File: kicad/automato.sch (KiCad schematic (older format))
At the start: 73 parts, among them J1 USB_C_Receptacle, J10 QWIIC 0, J11 UART2, J12 STEMMA 0, J2 LiPo, J3 Conn_01x07_Male, J4 Screw_Terminal_01x14, J5 USB_C_Receptacle, J6 Conn_Coaxial, J7 1-WIRE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

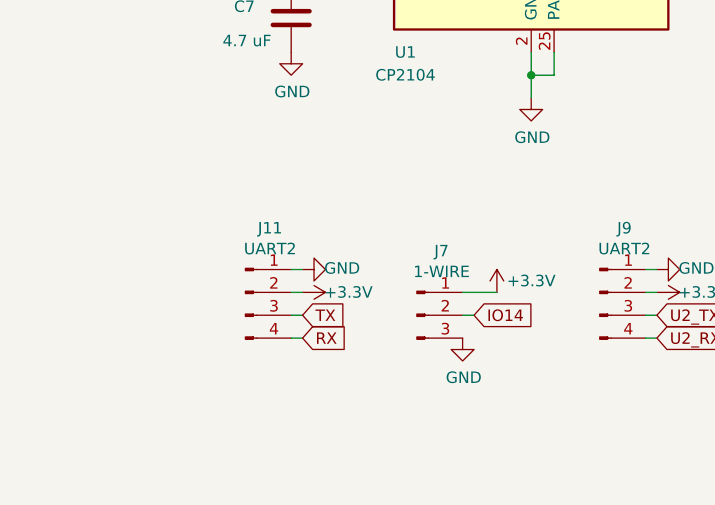
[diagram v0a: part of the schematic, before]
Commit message: remove usb-c uart JST
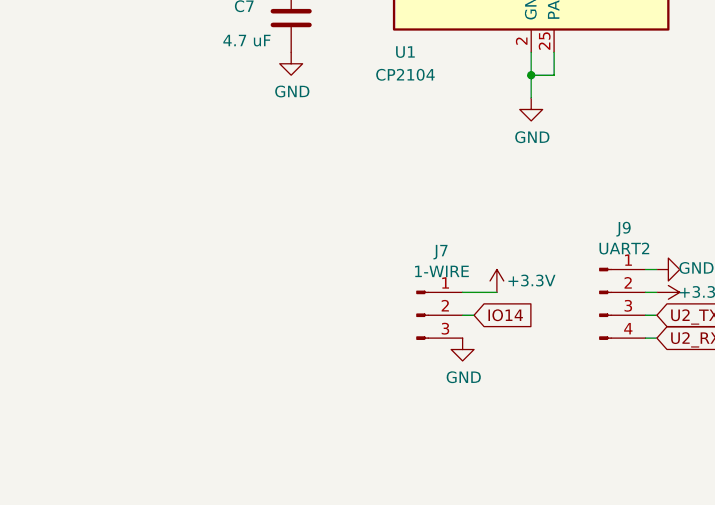
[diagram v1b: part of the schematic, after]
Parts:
- removed J11: UART2, Connector_JST:JST_PH_S4B-PH-SM4-TB_1x04-1MP_P2.00mm_Horizontal, symbol Connector:Conn_01x04_Male
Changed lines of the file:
@@
 	3500 9650 3450 9650
-$Comp
-L power:GND #PWR0114
-U 1 1 63277429
-P 1950 9350
-F 0 "#PWR0114" H 1950 9100 50  0001 C CNN
-F 1 "GND" V 1955 9177 50  0000 C CNN
-F 2 "" H 1950 9350 50  0001 C CNN
-F 3 "" H 1950 9350 50  0001 C CNN
-	1    1950 9350
-	0    -1   -1   0
-$EndComp
-Text GLabel 1950 9650 2    50   Input ~ 0
-RX
-Text GLabel 1950 9550 2    50   Input ~ 0
-TX
-Wire Wire Line
-	1950 9550 1900 9550
-Wire Wire Line
-	1950 9450 1900 9450
-$Comp
-L Connector:Conn_01x04_Male J11
-U 1 1 63277433
-P 1700 9450
-F 0 "J11" H 1808 9731 50  0000 C CNN
-F 1 "UART2" H 1808 9640 50  0000 C CNN
-F 2 "Connector_JST:JST_PH_S4B-PH-SM4-TB_1x04-1MP_P2.00mm_Horizontal" H 1700 9450 50  0001 C CNN
-F 3 "~" H 1700 9450 50  0001 C CNN
-	1    1700 9450
-	1    0    0    -1
-$EndComp
-$Comp
-L power:+3.3V #PWR0115
-U 1 1 63277439
-P 1950 9450
-F 0 "#PWR0115" H 1950 9300 50  0001 C CNN
-F 1 "+3.3V" V 1950 9650 50  0000 C CNN
-F 2 "" H 1950 9450 50  0001 C CNN
-F 3 "" H 1950 9450 50  0001 C CNN
-	1    1950 9450
-	0    1    1    0
-$EndComp
-Wire Wire Line
-	1900 9350 1950 9350
-Wire Wire Line
-	1950 9650 1900 9650
 $Comp
 L power:+3.3V #PWR0116

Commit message: add i2c and uart level shifting
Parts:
- added JP? (x3): SolderJumper_3_Bridged12, Jumper:SolderJumper-3_P1.3mm_Bridged12_RoundedPad1.0x1.5mm, symbol Jumper:SolderJumper_3_Bridged12
- added Q4, Q? (x4): Q_DUAL_NMOS_S1G1D2S2G2D1, Package_TO_SOT_SMD:SOT-23-6, symbol Device:Q_DUAL_NMOS_S1G1D2S2G2D1
- added Q?: Q_NMOS_GDS, symbol Device:Q_NMOS_GDS
- added RN1, RN? (x2): R_Pack02, Resistor_SMD:R_Array_Concave_2x0603, symbol Device:R_Pack02
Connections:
- wire segments 265 -> 304
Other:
- moved on the sheet: J10, J12, J4, J7, J9

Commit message: spaced out power supplies
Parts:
- gave numbers to parts that had none: 8
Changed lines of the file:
@@
 I2C_SCL
 $Comp
-L Jumper:SolderJumper_3_Bridged12 JP?
+L Jumper:SolderJumper_3_Bridged12 JP5
 U 1 1 6348EF51
 P 7450 9450
-F 0 "JP?" V 7404 9518 50  0000 L CNN
+F 0 "JP5" V 7404 9518 50  0000 L CNN
 F 1 "SolderJumper_3_Bridged12" V 7495 9518 50  0000 L CNN
 F 2 "Jumper:SolderJumper-3_P1.3mm_Bridged12_RoundedPad1.0x1.5mm" H 7450 9450 50  0001 C CNN
@@
 Connection ~ 7450 9600
 $Comp
-L power:+3.3V #PWR?
+L power:+3.3V #PWR0106
 U 1 1 634E420B
 P 7250 9250
-F 0 "#PWR?" H 7250 9100 50  0001 C CNN
+F 0 "#PWR0106" H 7250 9100 50  0001 C CNN
 F 1 "+3.3V" H 7400 9300 50  0000 C CNN
 F 2 "" H 7250 9250 50  0001 C CNN
@@
 	7100 10150 7700 10150
 $Comp
-L power:GND #PWR?
+L power:GND #PWR0107
 U 1 1 63571987
 P 4900 9850
-F 0 "#PWR?" H 4900 9600 50  0001 C CNN
+F 0 "#PWR0107" H 4900 9600 50  0001 C CNN
 F 1 "GND" V 4850 9850 50  0000 C CNN
 F 2 "" H 4900 9850 50  0001 C CNN
@@
 $EndComp
 $Comp
-L Device:Q_DUAL_NMOS_S1G1D2S2G2D1 Q?
+L Device:Q_DUAL_NMOS_S1G1D2S2G2D1 Q7
 U 1 1 6357198D
 P 5650 10050
-F 0 "Q?" V 5899 10050 50  0000 C CNN
+F 0 "Q7" V 5899 10050 50  0000 C CNN
 F 1 "Q_DUAL_NMOS_S1G1D2S2G2D1" V 5990 10050 50  0000 C CNN
 F 2 "Package_TO_SOT_SMD:SOT-23-6" H 5850 10050 50  0001 C CNN
@@
 	6200 10050 6250 10050
 $Comp
-L power:+3.3V #PWR?
+L power:+3.3V #PWR0108
 U 1 1 63571997
 P 5650 9600
-F 0 "#PWR?" H 5650 9450 50  0001 C CNN
+F 0 "#PWR0108" H 5650 9450 50  0001 C CNN
 F 1 "+3.3V" H 5800 9650 50  0000 C CNN
 F 2 "" H 5650 9600 50  0001 C CNN
@@
 	5650 9600 5650 9850
 $Comp
-L power:+3.3V #PWR?
+L power:+3.3V #PWR0110
 U 1 1 6357199E
 P 6000 9600
-F 0 "#PWR?" H 6000 9450 50  0001 C CNN
+F 0 "#PWR0110" H 6000 9450 50  0001 C CNN
 F 1 "+3.3V" H 6150 9650 50  0000 C CNN
 F 2 "" H 6000 9600 50  0001 C CNN
@@
 	5850 10150 6250 10150
 $Comp
-L Device:Q_DUAL_NMOS_S1G1D2S2G2D1 Q?
+L Device:Q_DUAL_NMOS_S1G1D2S2G2D1 Q7
 U 2 1 635719A9
 P 6000 9950
-F 0 "Q?" V 6249 9950 50  0000 C CNN
+F 0 "Q7" V 6249 9950 50  0000 C CNN
 F 1 "Q_DUAL_NMOS_S1G1D2S2G2D1" V 6340 9950 50  0000 C CNN
 F 2 "Package_TO_SOT_SMD:SOT-23-6" H 6200 9950 50  0001 C CNN
@@
 $EndComp
 $Comp
-L Device:R_Pack02 RN?
+L Device:R_Pack02 RN3
 U 1 1 635719AF
 P 5400 9800
-F 0 "RN?" H 5488 9846 50  0000 L CNN
+F 0 "RN3" H 5488 9846 50  0000 L CNN
 F 1 "R_Pack02" H 5488 9755 50  0000 L CNN
 F 2 "Resistor_SMD:R_Array_Concave_2x0603" V 5575 9800 50  0001 C CNN
@@
 I2C_SCL
 $Comp
-L Jumper:SolderJumper_3_Bridged12 JP?
+L Jumper:SolderJumper_3_Bridged12 JP4
 U 1 1 635719B7
 P 5050 9450
-F 0 "JP?" V 5004 9518 50  0000 L CNN
+F 0 "JP4" V 5004 9518 50  0000 L CNN
 F 1 "SolderJumper_3_Bridged12" V 5095 9518 50  0000 L CNN
 F 2 "Jumper:SolderJumper-3_P1.3mm_Bridged12_RoundedPad1.0x1.5mm" H 5050 9450 50  0001 C CNN
@@
 Connection ~ 5050 9600
 $Comp
-L power:+3.3V #PWR?
+L power:+3.3V #PWR0113
 U 1 1 635719C3
 P 4850 9250
-F 0 "#PWR?" H 4850 9100 50  0001 C CNN
+F 0 "#PWR0113" H 4850 9100 50  0001 C CNN
 F 1 "+3.3V" H 5000 9300 50  0000 C CNN
 F 2 "" H 4850 9250 50  0001 C CNN
@@
 	2400 9850 2600 9850
 $Comp
-L power:GND #PWR?
+L power:GND #PWR0118
 U 1 1 63640A07
 P 2600 9850
-F 0 "#PWR?" H 2600 9600 50  0001 C CNN
+F 0 "#PWR0118" H 2600 9600 50  0001 C CNN
 F 1 "GND" V 2550 9850 50  0000 C CNN
 F 2 "" H 2600 9850 50  0001 C CNN
@@
 $EndComp
 $Comp
-L Device:Q_DUAL_NMOS_S1G1D2S2G2D1 Q?
+L Device:Q_DUAL_NMOS_S1G1D2S2G2D1 Q6
 U 1 1 63640A0D
 P 3350 10050
-F 0 "Q?" V 3599 10050 50  0000 C CNN
+F 0 "Q6" V 3599 10050 50  0000 C CNN
 F 1 "Q_DUAL_NMOS_S1G1D2S2G2D1" V 3690 10050 50  0000 C CNN
 F 2 "Package_TO_SOT_SMD:SOT-23-6" H 3550 10050 50  0001 C CNN
@@
 	3900 10050 3950 10050
 $Comp
-L power:+3.3V #PWR?
+L power:+3.3V #PWR0119
 U 1 1 63640A17
 P 3350 9600
-F 0 "#PWR?" H 3350 9450 50  0001 C CNN
+F 0 "#PWR0119" H 3350 9450 50  0001 C CNN
 F 1 "+3.3V" H 3500 9650 50  0000 C CNN
 F 2 "" H 3350 9600 50  0001 C CNN
@@
 	3350 9600 3350 9850
 $Comp
-L power:+3.3V #PWR?
+L power:+3.3V #PWR0120
 U 1 1 63640A1E
 P 3700 9600
-F 0 "#PWR?" H 3700 9450 50  0001 C CNN
+F 0 "#PWR0120" H 3700 9450 50  0001 C CNN
 F 1 "+3.3V" H 3850 9650 50  0000 C CNN
 F 2 "" H 3700 9600 50  0001 C CNN
@@
 	3550 10150 3950 10150
 $Comp
-L Device:Q_DUAL_NMOS_S1G1D2S2G2D1 Q?
+L Device:Q_DUAL_NMOS_S1G1D2S2G2D1 Q6
 U 2 1 63640A29
 P 3700 9950
-F 0 "Q?" V 3949 9950 50  0000 C CNN
+F 0 "Q6" V 3949 9950 50  0000 C CNN
 F 1 "Q_DUAL_NMOS_S1G1D2S2G2D1" V 4040 9950 50  0000 C CNN
 F 2 "Package_TO_SOT_SMD:SOT-23-6" H 3900 9950 50  0001 C CNN
@@
 $EndComp
 $Comp
-L Device:R_Pack02 RN?
+L Device:R_Pack02 RN2
 U 1 1 63640A2F
 P 3100 9800
-F 0 "RN?" H 3188 9846 50  0000 L CNN
+F 0 "RN2" H 3188 9846 50  0000 L CNN
 F 1 "R_Pack02" H 3188 9755 50  0000 L CNN
 F 2 "Resistor_SMD:R_Array_Concave_2x0603" V 3275 9800 50  0001 C CNN
@@
 $EndComp
 $Comp
-L Jumper:SolderJumper_3_Bridged12 JP?
+L Jumper:SolderJumper_3_Bridged12 JP3
 U 1 1 63640A37
 P 2750 9450
-F 0 "JP?" V 2704 9518 50  0000 L CNN
+F 0 "JP3" V 2704 9518 50  0000 L CNN
 F 1 "SolderJumper_3_Bridged12" V 2795 9518 50  0000 L CNN
 F 2 "Jumper:SolderJumper-3_P1.3mm_Bridged12_RoundedPad1.0x1.5mm" H 2750 9450 50  0001 C CNN
@@
 Connection ~ 2750 9600
 $Comp
-L power:+3.3V #PWR?
+L power:+3.3V #PWR0121
 U 1 1 63640A43
 P 2550 9250
-F 0 "#PWR?" H 2550 9100 50  0001 C CNN
+F 0 "#PWR0121" H 2550 9100 50  0001 C CNN
 F 1 "+3.3V" H 2700 9300 50  0000 C CNN
 F 2 "" H 2550 9250 50  0001 C CNN
@@
 U2_RXD
 $Comp
-L Device:Q_NMOS_GDS Q?
+L Device:Q_NMOS_GDS Q5
 U 1 1 637094B9
 P 1400 9400
-F 0 "Q?" V 1649 9400 50  0000 C CNN
+F 0 "Q5" V 1649 9400 50  0000 C CNN
 F 1 "Q_NMOS_GDS" V 1740 9400 50  0000 C CNN
 F 2 "" H 1600 9500 50  0001 C CNN

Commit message: writing in wroom-da
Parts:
- removed Q5: Q_NMOS_GDS, symbol Device:Q_NMOS_GDS
- added U8: ESP32-WROOM-DA, automato-sensor:ESP32-WROOM-DA, symbol automato-sensor:ESP32-WROOM-DA
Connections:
- wire segments 304 -> 341

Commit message: playing with pins
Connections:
- net CS_RELAY: now also U8.17 (IO13); no longer U8.14 (IO12)
- net CS_SD: now also U8.14 (IO12); no longer U8.31 (IO5)
- net I2C_SCL: now also U8.38 (IO22); no longer U8.35 (IO21)
- net I2C_SDA: now also U8.35 (IO21); no longer U8.33 (IO19)
- net IO13: no longer U4.13 (IO14), U8.17 (IO13)
- net IO14: now also U4.13 (IO14); no longer U4.23 (IO15)
- net IO15: now also U4.23 (IO15); no longer JP1.3 (B), Q6.1 (S), U4.27 (IO16)
- net IO16: now also JP1.3 (B), Q6.1 (S), U4.27 (IO16); no longer JP2.3 (B), Q6.4 (S), U4.28 (IO17)
- net IRQ_LORA: now also U8.31 (IO5); no longer U8.9 (IO33)
- net RST_EINK: now also U8.9 (IO33); no longer U8.39 (IO23)
- net SPI_CLK: now also U8.32 (IO18); no longer U8.30 (IO17)
- net SPI_MISO: now also U8.33 (IO19); no longer U8.32 (IO18)
- net SPI_MOSI: now also U8.39 (IO23); no longer U8.38 (IO22)
- new net IO17: JP2.3 (B), Q6.4 (S), U4.28 (IO17), U8.30 (IO17)
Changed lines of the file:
@@
 CS_SD
 Text GLabel 9650 5850 2    50   Input ~ 0
+IO17
+Text GLabel 9650 5550 2    50   Input ~ 0
+IO14
+Text GLabel 9650 5650 2    50   Input ~ 0
+IO15
+Text GLabel 9650 5750 2    50   Input ~ 0
 IO16
-Text GLabel 9650 5550 2    50   Input ~ 0
-IO13
-Text GLabel 9650 5650 2    50   Input ~ 0
-IO14
-Text GLabel 9650 5750 2    50   Input ~ 0
-IO15
 Text GLabel 9900 5850 2    50   Input ~ 0
 U2_TXD
@@
 Text GLabel 19900 6500 2    50   Input ~ 0
 CS_EINK
+Text GLabel 19900 6750 2    50   Input ~ 0
+RST_EINK
+Wire Wire Line
+	19800 6750 19900 6750
+Wire Wire Line
+	19800 6200 19900 6200
 Text GLabel 19900 6200 2    50   Input ~ 0
-RST_EINK
-Wire Wire Line
-	19800 6200 19900 6200
-Wire Wire Line
-	19800 6100 19900 6100
+SPI_MOSI
 Text GLabel 19900 6100 2    50   Input ~ 0
-SPI_MOSI
+I2C_SCL
 Text GLabel 19900 6000 2    50   Input ~ 0
-I2C_SCL
-Text GLabel 19900 5850 2    50   Input ~ 0
 I2C_SDA
 Wire Wire Line
@@
 IO16
 Wire Wire Line
+	19800 5850 19900 5850
+Wire Wire Line
 	19800 5750 19900 5750
-Wire Wire Line
-	19800 5650 19900 5650
+Text GLabel 19900 5850 2    50   Input ~ 0
+SPI_MISO
 Text GLabel 19900 5750 2    50   Input ~ 0
-SPI_MISO
-Text GLabel 19900 5650 2    50   Input ~ 0
 SPI_CLK
-Wire Wire Line
-	19800 5450 20150 5450
 Text GLabel 19900 5350 2    50   Input ~ 0
 IO14
@@
 Wire Wire Line
 	19800 5350 19900 5350
-Text GLabel 19900 5000 2    50   Input ~ 0
+Text GLabel 19900 5150 2    50   Input ~ 0
 CS_SD
+Text GLabel 19900 5650 2    50   Input ~ 0
+IO17
 Text GLabel 19900 5250 2    50   Input ~ 0
-IO13
-Text GLabel 19900 5150 2    50   Input ~ 0
 CS_RELAY
 Wire Wire Line
@@
 	19800 5150 19900 5150
 Wire Wire Line
+	19800 4900 19900 4900
+Wire Wire Line
 	19800 5000 19900 5000
-Wire Wire Line
-	19800 4900 19900 4900
-Wire Wire Line
-	19800 6750 19900 6750
 Text GLabel 19900 4900 2    50   Input ~ 0
 CS_LORA
-Text GLabel 19900 6750 2    50   Input ~ 0
+Text GLabel 19900 5000 2    50   Input ~ 0
 IRQ_LORA
 Wire Wire Line
@@
 	18900 7250 18950 7250
 $Comp
-L power:+3.3V #PWR?
+L power:+3.3V #PWR0122
 U 1 1 6371B3EA
 P 19250 3700
-F 0 "#PWR?" H 19250 3550 50  0001 C CNN
+F 0 "#PWR0122" H 19250 3550 50  0001 C CNN
 F 1 "+3.3V" H 19265 3873 50  0000 C CNN
 F 2 "" H 19250 3700 50  0001 C CNN
@@
 	1    0    0    -1
 $EndComp
+Text GLabel 20150 5650 2    50   Input ~ 0
+U2_TXD
 Text GLabel 20150 5550 2    50   Input ~ 0
-U2_TXD
-Text GLabel 20150 5450 2    50   Input ~ 0
 U2_RXD
 Text GLabel 10800 6850 2    50   Input ~ 0
 IO14
 Wire Wire Line
+	19800 6100 19900 6100
+Wire Wire Line
 	19800 6000 19900 6000
-Wire Wire Line
-	19800 5850 19900 5850
 $Comp
 L automato-sensor:ESP32-WROOM-DA U8
@@
 Wire Wire Line
 	19250 3700 19250 4500
+Wire Wire Line
+	19800 5450 19900 5450
+Wire Wire Line
+	19800 5650 20150 5650
 $EndSCHEMATC

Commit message: swapping to wroom-da
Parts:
- removed J3: Conn_01x07_Male, Connector_PinHeader_2.54mm:PinHeader_1x07_P2.54mm_Vertical, symbol Connector:Conn_01x07_Male
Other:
- moved on the sheet: C5, J6, R6, U3, U5, U8

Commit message: update
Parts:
- removed U4: ESP32-WROOM-32D, RF_Module:ESP32-WROOM-32, symbol automato-rescue:ESP32-WROOM-32D-RF_Module
- renumbered U8 to U4
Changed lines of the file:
@@
 Text GLabel 8250 5050 0    50   Input ~ 0
 A1
-$Comp
-L automato-rescue:ESP32-WROOM-32D-RF_Module U4
-U 1 1 5FB06A02
-P 8950 5950
-F 0 "U4" H 8200 4650 50  0000 C CNN
-F 1 "ESP32-WROOM-32D" H 8200 4550 50  0000 C CNN
-F 2 "RF_Module:ESP32-WROOM-32" H 8950 4450 50  0001 C CNN
-F 3 "https://www.espressif.com/sites/default/files/documentation/esp32-wroom-32d_esp32-wroom-32u_datasheet_en.pdf" H 8650 6000 50  0001 C CNN
-	1    8950 5950
-	1    0    0    -1
-$EndComp
 Wire Wire Line
 	11250 5250 11600 5250
@@
 	12900 6300 13000 6300
 $Comp
-L automato-sensor:ESP32-WROOM-DA U8
+L automato-sensor:ESP32-WROOM-DA U4
 U 1 1 630997BE
 P 12450 6650
-F 0 "U8" H 11750 8450 50  0000 C CNN
+F 0 "U4" H 11750 8450 50  0000 C CNN
 F 1 "ESP32-WROOM-DA" H 12550 5850 50  0000 C CNN
 F 2 "automato-sensor:ESP32-WROOM-DA" H 12300 7350 50  0001 C CNN
